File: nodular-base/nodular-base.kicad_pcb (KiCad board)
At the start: 4 copper layers, 83.1 x 92.5 mm, 64 parts, among them J1 Conn_02x10_Counter_Clockwise, J2 Conn_02x10_Counter_Clockwise, J3 Conn_02x10_Counter_Clockwise, J4 Conn_02x10_Counter_Clockwise, J5 Conn_02x10_Counter_Clockwise, J6 Conn_02x10_Counter_Clockwise, J7 USB_C_Receptacle_USB2.0, J8 USB_C_Receptacle_USB2.0, J9 Conn_01x30_MountingPin, SW1 SW_Push, SW2 SW_Push, SW3 SW_Push, U1 ESP32-S3-PICO-1-N8R2, U10 MT9700, U11 MT9700, U12 MT9700, U13 MT9700, U14 MT9700, U2 FUSB302BMPX, U3 BQ25895RTW, U4 TCA9548APWR, U5 MAX3051, U6 74LVC1G17, U7 SC7A20, U8 MT9700, U9 MT9700

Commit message: WIP layout for base
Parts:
- removed the REF** at (99.9, 126.2)
- removed the REF** at (83.7, 100.0)
- removed the REF** at (90.7, 110.5)
- removed the REF** at (113.7, 107.1)
- removed the REF** at (78.8, 112.0)
- removed the REF** at (87.8, 101.5)
- removed the REF** at (79.0, 82.2)
- added C10: 10uF, Capacitor_SMD:C_1206_3216Metric, F.Cu at (119.8, 83.8)
- added C11: 10uF, Capacitor_SMD:C_1206_3216Metric, F.Cu at (122.5, 87.4)
- added C12: 10uF, Capacitor_SMD:C_1206_3216Metric, F.Cu at (118.1, 106.0)
- added C13: 10uF, Capacitor_SMD:C_1206_3216Metric, F.Cu at (119.1, 97.9)
- added C14: 10uF, Capacitor_SMD:C_1206_3216Metric, F.Cu at (118.1, 108.4)
- added C15: 10uF, Capacitor_SMD:C_1206_3216Metric, F.Cu at (120.2, 117.2)
- added C16: 100nF, Capacitor_SMD:C_0402_1005Metric, F.Cu at (126.6, 92.7)
- added C17: 10uF, Capacitor_SMD:C_1206_3216Metric, F.Cu at (102.6, 124.0)
- added C18: 10uF, Capacitor_SMD:C_1206_3216Metric, F.Cu at (96.0, 124.0)
- added C19: 10uF, Capacitor_SMD:C_1206_3216Metric, F.Cu at (80.7, 114.1)
- added C20: 10uF, Capacitor_SMD:C_1206_3216Metric, F.Cu at (77.5, 107.5)
- added C21: 10uF, Capacitor_SMD:C_1206_3216Metric, F.Cu at (83.0, 89.8)
- added C22: 10uF, Capacitor_SMD:C_1206_3216Metric, F.Cu at (82.5, 84.7)
- added C23: 10uF, Capacitor_SMD:C_1206_3216Metric, F.Cu at (86.9, 93.0)
- added C24: 10uF, Capacitor_SMD:C_1206_3216Metric, F.Cu at (87.0, 86.5)
- added C25: 4.7uF, Capacitor_SMD:C_0603_1608Metric, F.Cu at (89.9, 99.2)
- added C26: 47nF, Capacitor_SMD:C_0402_1005Metric, F.Cu at (88.9, 101.0)
- added C27: 10uF, Capacitor_SMD:C_1206_3216Metric, F.Cu at (86.8, 107.8)
- added C28: 10uF, Capacitor_SMD:C_1206_3216Metric, F.Cu at (82.1, 106.8)
- added C29: 10uF, Capacitor_SMD:C_1206_3216Metric, F.Cu at (81.8, 103.3)
- added C30: 1uF, Capacitor_SMD:C_0603_1608Metric, F.Cu at (87.2, 95.8)
- added C31: 47nF, Capacitor_SMD:C_0402_1005Metric, F.Cu at (84.8, 110.2)
- added C32: 10uF, Capacitor_SMD:C_1206_3216Metric, F.Cu at (91.6, 107.8)
- added C33: 10uF, Capacitor_SMD:C_1206_3216Metric, F.Cu at (91.7, 115.3)
- added C34: 10uF, Capacitor_SMD:C_1206_3216Metric, F.Cu at (90.2, 112.9)
- added C9: 22uF, Capacitor_SMD:C_1206_3216Metric, F.Cu at (107.6, 66.9)
- added D2: SK6805MICRO-J, LED_SMD:LED_SK6805_PLCC4_2.4x2.7mm_P1.3mm, F.Cu at (97.0, 80.8)
- added L2: L, Inductor_SMD_Wurth:L_Wurth_WE-LQSH-4020, F.Cu at (86.9, 104.2)
- added L3: L, Inductor_SMD_Wurth:L_Wurth_WE-LQSH-2512, F.Cu at (91.0, 110.3)
- added R10: 10k, Resistor_SMD:R_0402_1005Metric, F.Cu at (126.2, 117.2)
- added R11: 11k3, Resistor_SMD:R_0402_1005Metric, F.Cu at (121.0, 113.6)
- added R12: R, Resistor_SMD:R_0402_1005Metric, F.Cu at (124.5, 83.7)
- added R13: R, Resistor_SMD:R_0603_1608Metric, F.Cu at (127.5, 83.5)
- added R14: 100k, Resistor_SMD:R_0402_1005Metric, F.Cu at (93.3, 130.2)
- added R15: 10k, Resistor_SMD:R_0402_1005Metric, F.Cu at (91.3, 130.2)
- added R16: 11k3, Resistor_SMD:R_0402_1005Metric, F.Cu at (98.2, 125.7)
- added R17: 100k, Resistor_SMD:R_0402_1005Metric, F.Cu at (77.3, 113.7)
- added R18: 10k, Resistor_SMD:R_0402_1005Metric, F.Cu at (72.8, 106.8)
- added R19: 11k3, Resistor_SMD:R_0402_1005Metric, F.Cu at (75.7, 109.7)
- added R20: 100k, Resistor_SMD:R_0402_1005Metric, F.Cu at (75.1, 92.5)
- added R21: 10k, Resistor_SMD:R_0402_1005Metric, F.Cu at (70.1, 92.7)
- added R22: 11k3, Resistor_SMD:R_0402_1005Metric, F.Cu at (80.8, 90.2)
- added R23: 11k3, Resistor_SMD:R_0402_1005Metric, F.Cu at (85.3, 88.6)
- added R24: 1k, Resistor_SMD:R_0402_1005Metric, F.Cu at (97.8, 78.5)
- added R25: 11k3, Resistor_SMD:R_0402_1005Metric, F.Cu at (85.3, 90.7)
- added R26: 1k, Resistor_SMD:R_0402_1005Metric, F.Cu at (99.5, 82.8)
- added R27: 2k2, Resistor_SMD:R_0402_1005Metric, F.Cu at (75.4, 73.7)
- added R28: R, Resistor_SMD:R_0402_1005Metric, F.Cu at (85.8, 110.2)
- added R29: 10k, Resistor_SMD:R_0402_1005Metric, F.Cu at (82.5, 95.5)
- added R3: 11k3, Resistor_SMD:R_0402_1005Metric, F.Cu at (116.2, 87.8)
- added R30: 10k, Resistor_SMD:R_0402_1005Metric, F.Cu at (90.5, 101.0)
- added R31: 10k, Resistor_SMD:R_0402_1005Metric, F.Cu at (91.6, 101.0)
- added R32: R, Resistor_SMD:R_0402_1005Metric, F.Cu at (87.2, 112.1)
- added R4: 100k, Resistor_SMD:R_0402_1005Metric, F.Cu at (116.7, 89.6)
- added R5: 10k, Resistor_SMD:R_0402_1005Metric, F.Cu at (116.7, 90.7)
- added R6: 100k, Resistor_SMD:R_0402_1005Metric, F.Cu at (135.2, 93.9)
- added R7: 10k, Resistor_SMD:R_0402_1005Metric, F.Cu at (132.8, 95.4)
- added R8: 11k3, Resistor_SMD:R_0402_1005Metric, F.Cu at (116.8, 99.5)
- added R9: 100k, Resistor_SMD:R_0402_1005Metric, F.Cu at (124.2, 114.5)
- added REF**: Diodes_UDFN-10_1.0x2.5mm_P0.5mm, Package_DFN_QFN:Diodes_UDFN-10_1.0x2.5mm_P0.5mm, F.Cu at (100.8, 84.2)
- added REF**: Diodes_UDFN-10_1.0x2.5mm_P0.5mm, Package_DFN_QFN:Diodes_UDFN-10_1.0x2.5mm_P0.5mm, F.Cu at (103.9, 84.2)
- added REF**: Diodes_UDFN-10_1.0x2.5mm_P0.5mm, Package_DFN_QFN:Diodes_UDFN-10_1.0x2.5mm_P0.5mm, F.Cu at (93.7, 84.0)
- added REF**: Diodes_UDFN-10_1.0x2.5mm_P0.5mm, Package_DFN_QFN:Diodes_UDFN-10_1.0x2.5mm_P0.5mm, F.Cu at (96.8, 84.0)
- added U15: 74LVC1G04, Package_TO_SOT_SMD:SOT-353_SC-70-5, F.Cu at (119.4, 90.5)
- added U16: RCLAMP0524P-ES, Package_DFN_QFN:Diodes_UDFN-10_1.0x2.5mm_P0.5mm, F.Cu at (106.1, 74.7)
- added U17: RCLAMP0524P-ES, Package_DFN_QFN:Diodes_UDFN-10_1.0x2.5mm_P0.5mm, F.Cu at (120.5, 79.5)
- added U18: RCLAMP0524P-ES, Package_DFN_QFN:Diodes_UDFN-10_1.0x2.5mm_P0.5mm, F.Cu at (109.2, 69.3)
- added U19: 74LVC1G04, Package_TO_SOT_SMD:SOT-353_SC-70-5, F.Cu at (133.2, 93.2)
- added U20: RCLAMP0524P-ES, Package_DFN_QFN:Diodes_UDFN-10_1.0x2.5mm_P0.5mm, F.Cu at (119.3, 93.7)
- added U21: RCLAMP0524P-ES, Package_DFN_QFN:Diodes_UDFN-10_1.0x2.5mm_P0.5mm, F.Cu at (133.0, 101.3)
- added U22: RCLAMP0524P-ES, Package_DFN_QFN:Diodes_UDFN-10_1.0x2.5mm_P0.5mm, F.Cu at (133.0, 98.2)
- added U23: 74LVC1G04, Package_TO_SOT_SMD:SOT-353_SC-70-5, F.Cu at (124.2, 116.8)
- added U24: AW9523B, Package_DFN_QFN:QFN-24-1EP_4x4mm_P0.5mm_EP2.7x2.6mm, F.Cu at (77.2, 120.2)
- added U25: AW9523B, Package_DFN_QFN:QFN-24-1EP_4x4mm_P0.5mm_EP2.7x2.6mm, F.Cu at (125.8, 109.6)
- added U26: AW9523B, Package_DFN_QFN:QFN-24-1EP_4x4mm_P0.5mm_EP2.7x2.6mm, F.Cu at (137.6, 99.9)
- added U27: RCLAMP0524P-ES, Package_DFN_QFN:Diodes_UDFN-10_1.0x2.5mm_P0.5mm, F.Cu at (117.2, 128.8)
- added U28: RCLAMP0524P-ES, Package_DFN_QFN:Diodes_UDFN-10_1.0x2.5mm_P0.5mm, F.Cu at (120.9, 120.4)
- added U29: RCLAMP0524P-ES, Package_DFN_QFN:Diodes_UDFN-10_1.0x2.5mm_P0.5mm, F.Cu at (113.8, 113.1)
- added U30: RCLAMP0524P-ES, Package_DFN_QFN:Diodes_UDFN-10_1.0x2.5mm_P0.5mm, F.Cu at (89.9, 67.2)
- added U31: 74LVC1G04, Package_TO_SOT_SMD:SOT-353_SC-70-5, F.Cu at (95.3, 128.1)
- added U32: 74LVC1G04, Package_TO_SOT_SMD:SOT-353_SC-70-5, F.Cu at (73.5, 108.8)
- added U33: 74LVC1G04, Package_TO_SOT_SMD:SOT-353_SC-70-5, F.Cu at (72.8, 92.0)
- added U34: RCLAMP0524P-ES, Package_DFN_QFN:Diodes_UDFN-10_1.0x2.5mm_P0.5mm, F.Cu at (82.7, 128.5)
- added U35: RCLAMP0524P-ES, Package_DFN_QFN:Diodes_UDFN-10_1.0x2.5mm_P0.5mm, F.Cu at (85.7, 130.4)
- added U36: RCLAMP0524P-ES, Package_DFN_QFN:Diodes_UDFN-10_1.0x2.5mm_P0.5mm, F.Cu at (85.0, 113.2)
- added U37: RCLAMP0524P-ES, Package_DFN_QFN:Diodes_UDFN-10_1.0x2.5mm_P0.5mm, F.Cu at (67.1, 98.5)
- added U38: RCLAMP0524P-ES, Package_DFN_QFN:Diodes_UDFN-10_1.0x2.5mm_P0.5mm, F.Cu at (67.1, 101.8)
- added U39: RCLAMP0524P-ES, Package_DFN_QFN:Diodes_UDFN-10_1.0x2.5mm_P0.5mm, F.Cu at (80.7, 99.3)
- added U40: RCLAMP0524P-ES, Package_DFN_QFN:Diodes_UDFN-10_1.0x2.5mm_P0.5mm, F.Cu at (91.3, 70.0)
- added U41: RCLAMP0524P-ES, Package_DFN_QFN:Diodes_UDFN-10_1.0x2.5mm_P0.5mm, F.Cu at (79.9, 80.0)
- added U42: RCLAMP0524P-ES, Package_DFN_QFN:Diodes_UDFN-10_1.0x2.5mm_P0.5mm, F.Cu at (95.3, 77.3)
- added U43: TLV62595DMQR, nodular:Texas_VSON-HR-6_1.5x1.5mm_P0.5mm, F.Cu at (88.1, 110.0)
- J10: renamed from REF**; value JST_PH_B2B-PH-SM4-TB_1x02-1MP_P2.00mm_Vertical -> Conn_01x02
- moved U4 27.5 mm to (104.5, 131.3), turned to 180 degrees
- moved J3 26.1 mm to (113.0, 122.6), turned to 120 degrees
- moved J6 26.1 mm to (87.0, 77.4), turned to -60 degrees
- moved J1 26.1 mm to (113.0, 77.4), turned to -120 degrees
- moved J2 26.1 mm to (126.1, 100.0), turned to 180 degrees
- moved J4 26.1 mm to (87.0, 122.6), turned to 60 degrees
- moved J5 26.1 mm to (73.9, 100.0), turned to 0 degrees
- moved U11 23.6 mm to (99.3, 123.3)
- moved R2 19.5 mm to (92.0, 65.0), turned to 0 degrees
- moved U3 19.0 mm to (85.7, 99.2), turned to -90 degrees
- moved U13 18.8 mm to (79.8, 87.5), turned to -90 degrees
- moved R1 18.1 mm to (92.0, 66.0), turned to 0 degrees
- moved U6 17.2 mm to (100.6, 79.5), turned to -45 degrees
- moved U9 17.1 mm to (118.5, 102.6), turned to -90 degrees
- moved U10 9.19 mm to (118.8, 112.5), turned to 90 degrees
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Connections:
- net Net-(J7-CC1) renamed /USB/CC1
- net Net-(J7-CC2) renamed /USB/CC2
- net Net-(U3-SYS-Pad15) renamed /USB/VSYS
- C3 pad 1: Net-(U1-VDD3P3_CPU) -> 3V3_SYS
- C4 pad 1: Net-(U1-VDD3P3_CPU) -> 3V3_SYS
- C5 pad 1: Net-(U1-VDD3P3_CPU) -> 3V3_SYS
- C6 pad 1: Net-(U1-VDD3P3_CPU) -> 3V3_SYS
- C7 pad 1: Net-(U1-VDD3P3_CPU) -> 3V3_SYS
- C8 pad 1: Net-(U1-VDD3P3_CPU) -> 3V3_SYS
- D1 pad 1: unconnected-(D1-K-Pad1) -> /USB/STAT
- D1 pad 2: unconnected-(D1-A-Pad2) -> Net-(D1-A)
- J1 pad 12: unconnected-(J1-Pin_12-Pad12) -> /NA_HS1
- J1 pad 13: unconnected-(J1-Pin_13-Pad13) -> /NA_HS2
- J1 pad 15: unconnected-(J1-Pin_15-Pad15) -> /SFPs/PORTA_3V3
- J1 pad 16: unconnected-(J1-Pin_16-Pad16) -> /SFPs/PORTA_3V3
- J1 pad 18: unconnected-(J1-Pin_18-Pad18) -> /NA_HS3
- J1 pad 19: unconnected-(J1-Pin_19-Pad19) -> /NA_HS4
- J1 pad 2: unconnected-(J1-Pin_2-Pad2) -> /GPIO/ALS1
- J1 pad 3: unconnected-(J1-Pin_3-Pad3) -> /GPIO/ALS2
- J1 pad 4: unconnected-(J1-Pin_4-Pad4) -> /I2C/SDA_A
- J1 pad 5: unconnected-(J1-Pin_5-Pad5) -> /I2C/SCL_A
- J1 pad 6: unconnected-(J1-Pin_6-Pad6) -> /SFPs/A_NDET
- J1 pad 7: unconnected-(J1-Pin_7-Pad7) -> /GPIO/ALS3
- J1 pad 8: unconnected-(J1-Pin_8-Pad8) -> /GPIO/ALS4
- J1 pad 9: unconnected-(J1-Pin_9-Pad9) -> /GPIO/ALS5
- J10 pad 1: (no net) -> /USB/BAT+
- J10 pad 2: (no net) -> GND
- J2 pad 12: unconnected-(J2-Pin_12-Pad12) -> /NB_HS1
- J2 pad 13: unconnected-(J2-Pin_13-Pad13) -> /NB_HS2
- J2 pad 15: unconnected-(J2-Pin_15-Pad15) -> /SFPs/PORTB_3V3
- J2 pad 16: unconnected-(J2-Pin_16-Pad16) -> /SFPs/PORTB_3V3
- J2 pad 18: unconnected-(J2-Pin_18-Pad18) -> /NB_HS3
- J2 pad 19: unconnected-(J2-Pin_19-Pad19) -> /NB_HS4
- J2 pad 2: unconnected-(J2-Pin_2-Pad2) -> /GPIO/BLS1
- J2 pad 3: unconnected-(J2-Pin_3-Pad3) -> /GPIO/BLS2
- J2 pad 4: unconnected-(J2-Pin_4-Pad4) -> /I2C/SDA_B
- J2 pad 5: unconnected-(J2-Pin_5-Pad5) -> /I2C/SCL_B
- J2 pad 6: unconnected-(J2-Pin_6-Pad6) -> /SFPs/B_NDET
- J2 pad 7: unconnected-(J2-Pin_7-Pad7) -> /GPIO/BLS3
- J2 pad 8: unconnected-(J2-Pin_8-Pad8) -> /GPIO/BLS4
- J2 pad 9: unconnected-(J2-Pin_9-Pad9) -> /GPIO/BLS5
- J3 pad 12: unconnected-(J3-Pin_12-Pad12) -> /NC_HS1
- J3 pad 13: unconnected-(J3-Pin_13-Pad13) -> /NC_HS2
- J3 pad 15: unconnected-(J3-Pin_15-Pad15) -> /SFPs/PORTC_3V3
- J3 pad 16: unconnected-(J3-Pin_16-Pad16) -> /SFPs/PORTC_3V3
- J3 pad 18: unconnected-(J3-Pin_18-Pad18) -> /NC_HS3
- J3 pad 19: unconnected-(J3-Pin_19-Pad19) -> /NC_HS4
- J3 pad 2: unconnected-(J3-Pin_2-Pad2) -> /GPIO/CLS1
- J3 pad 3: unconnected-(J3-Pin_3-Pad3) -> /GPIO/CLS2
- J3 pad 4: unconnected-(J3-Pin_4-Pad4) -> /I2C/SDA_C
- J3 pad 5: unconnected-(J3-Pin_5-Pad5) -> /I2C/SCL_C
- J3 pad 6: unconnected-(J3-Pin_6-Pad6) -> /SFPs/C_NDET
- J3 pad 7: unconnected-(J3-Pin_7-Pad7) -> /GPIO/CLS3
- J3 pad 8: unconnected-(J3-Pin_8-Pad8) -> /GPIO/CLS4
- J3 pad 9: unconnected-(J3-Pin_9-Pad9) -> /GPIO/CLS5
- J4 pad 12: unconnected-(J4-Pin_12-Pad12) -> /ND_HS1
- J4 pad 13: unconnected-(J4-Pin_13-Pad13) -> /ND_HS2
- J4 pad 15: unconnected-(J4-Pin_15-Pad15) -> /SFPs/PORTD_3V3
- J4 pad 16: unconnected-(J4-Pin_16-Pad16) -> /SFPs/PORTD_3V3
- J4 pad 18: unconnected-(J4-Pin_18-Pad18) -> /ND_HS3
- J4 pad 19: unconnected-(J4-Pin_19-Pad19) -> /ND_HS4
- J4 pad 2: unconnected-(J4-Pin_2-Pad2) -> /GPIO/DLS1
- J4 pad 3: unconnected-(J4-Pin_3-Pad3) -> /GPIO/DLS2
- J4 pad 4: unconnected-(J4-Pin_4-Pad4) -> /I2C/SDA_D
- J4 pad 5: unconnected-(J4-Pin_5-Pad5) -> /I2C/SCL_D
- J4 pad 6: unconnected-(J4-Pin_6-Pad6) -> /SFPs/D_NDET
- J4 pad 7: unconnected-(J4-Pin_7-Pad7) -> /GPIO/DLS3
- J4 pad 8: unconnected-(J4-Pin_8-Pad8) -> /GPIO/DLS4
- J4 pad 9: unconnected-(J4-Pin_9-Pad9) -> /GPIO/DLS5
- J5 pad 12: unconnected-(J5-Pin_12-Pad12) -> /NE_HS1
- J5 pad 13: unconnected-(J5-Pin_13-Pad13) -> /NE_HS2
- J5 pad 15: unconnected-(J5-Pin_15-Pad15) -> /SFPs/PORTE_3V3
- J5 pad 16: unconnected-(J5-Pin_16-Pad16) -> /SFPs/PORTE_3V3
- J5 pad 18: unconnected-(J5-Pin_18-Pad18) -> /NE_HS3
- J5 pad 19: unconnected-(J5-Pin_19-Pad19) -> /NE_HS4
- J5 pad 2: unconnected-(J5-Pin_2-Pad2) -> /GPIO/ELS1
- J5 pad 3: unconnected-(J5-Pin_3-Pad3) -> /GPIO/ELS2
- J5 pad 4: unconnected-(J5-Pin_4-Pad4) -> /I2C/SDA_E
- J5 pad 5: unconnected-(J5-Pin_5-Pad5) -> /I2C/SCL_E
- J5 pad 6: unconnected-(J5-Pin_6-Pad6) -> /SFPs/E_NDET
- J5 pad 7: unconnected-(J5-Pin_7-Pad7) -> /GPIO/ELS3
- J5 pad 8: unconnected-(J5-Pin_8-Pad8) -> /GPIO/ELS4
- J5 pad 9: unconnected-(J5-Pin_9-Pad9) -> /GPIO/ELS5
- J6 pad 12: unconnected-(J6-Pin_12-Pad12) -> /NF_HS1
- J6 pad 13: unconnected-(J6-Pin_13-Pad13) -> /NF_HS2
- J6 pad 15: unconnected-(J6-Pin_15-Pad15) -> /SFPs/PORTF_3V3
- J6 pad 16: unconnected-(J6-Pin_16-Pad16) -> /SFPs/PORTF_3V3
- J6 pad 18: unconnected-(J6-Pin_18-Pad18) -> /NF_HS3
- J6 pad 19: unconnected-(J6-Pin_19-Pad19) -> /NF_HS4
- J6 pad 2: unconnected-(J6-Pin_2-Pad2) -> /GPIO/FLS1
- J6 pad 3: unconnected-(J6-Pin_3-Pad3) -> /GPIO/FLS2
- J6 pad 4: unconnected-(J6-Pin_4-Pad4) -> /I2C/SDA_F
- J6 pad 5: unconnected-(J6-Pin_5-Pad5) -> /I2C/SCL_F
- J6 pad 6: unconnected-(J6-Pin_6-Pad6) -> /SFPs/F_NDET
- J6 pad 7: unconnected-(J6-Pin_7-Pad7) -> /GPIO/FLS3
- J6 pad 8: unconnected-(J6-Pin_8-Pad8) -> /GPIO/FLS4
- J6 pad 9: unconnected-(J6-Pin_9-Pad9) -> /GPIO/FLS5
- J7 pad A4: Net-(U2-VBUS) -> /USB/VBUS
- J7 pad A9: Net-(U2-VBUS) -> /USB/VBUS
- J7 pad B4: Net-(U2-VBUS) -> /USB/VBUS
- J7 pad B9: Net-(U2-VBUS) -> /USB/VBUS
- J8 pad A1: Net-(J8-GND-PadA1) -> GND
- J8 pad A12: Net-(J8-GND-PadA1) -> GND
- J8 pad A4: Net-(J8-VBUS-PadA4) -> unconnected-(J8-VBUS-PadA4)
- J8 pad A6: unconnected-(J8-D+-PadA6) -> Net-(J8-D+-PadA6)
- J8 pad A7: unconnected-(J8-D--PadA7) -> Net-(J8-D--PadA7)
- J8 pad A9: Net-(J8-VBUS-PadA4) -> unconnected-(J8-VBUS-PadA4)
- J8 pad B1: Net-(J8-GND-PadA1) -> GND
- J8 pad B12: Net-(J8-GND-PadA1) -> GND
- J8 pad B4: Net-(J8-VBUS-PadA4) -> unconnected-(J8-VBUS-PadA4)
- J8 pad B6: unconnected-(J8-D+-PadB6) -> Net-(J8-D+-PadA6)
- J8 pad B7: unconnected-(J8-D--PadB7) -> Net-(J8-D--PadA7)
- J8 pad B9: Net-(J8-VBUS-PadA4) -> unconnected-(J8-VBUS-PadA4)
- J8 pad S1: unconnected-(J8-SHIELD-PadS1) -> GND
- U1 pad 10: unconnected-(U1-GPIO5-Pad10) -> /NF_HS3
- U1 pad 11: unconnected-(U1-GPIO6-Pad11) -> /NF_HS4
- U1 pad 16: unconnected-(U1-GPIO11-Pad16) -> /ND_HS1
- U1 pad 17: unconnected-(U1-GPIO12-Pad17) -> /ND_HS4
- U1 pad 18: unconnected-(U1-GPIO13-Pad18) -> /ND_HS3
- U1 pad 19: unconnected-(U1-GPIO14-Pad19) -> /ND_HS2
- U1 pad 2: Net-(U1-VDD3P3_CPU) -> 3V3_SYS
- U1 pad 20: Net-(U1-VDD3P3_CPU) -> 3V3_SYS
- U1 pad 21: unconnected-(U1-GPIO15-Pad21) -> /NE_HS3
- U1 pad 22: unconnected-(U1-GPIO16-Pad22) -> /NE_HS2
- U1 pad 23: unconnected-(U1-GPIO17-Pad23) -> /NE_HS4
- U1 pad 24: unconnected-(U1-GPIO18-Pad24) -> /NE_HS1
- U1 pad 27: unconnected-(U1-GPIO21-Pad27) -> /LED_DATA
- U1 pad 3: Net-(U1-VDD3P3_CPU) -> 3V3_SYS
- U1 pad 36: unconnected-(U1-GPIO48/SPICLK_n-Pad36) -> /NC_HS4
- U1 pad 37: unconnected-(U1-GPIO47/SPICLK_P-Pad37) -> /NC_HS3
- U1 pad 38: unconnected-(U1-GPIO33-Pad38) -> /NC_HS2
- U1 pad 39: unconnected-(U1-GPIO34-Pad39) -> /NC_HS1
- U1 pad 40: unconnected-(U1-GPIO35-Pad40) -> /NB_HS1
- U1 pad 41: unconnected-(U1-GPIO36-Pad41) -> /NB_HS2
- U1 pad 42: unconnected-(U1-GPIO37-Pad42) -> /NB_HS3
- U1 pad 43: unconnected-(U1-GPIO38-Pad43) -> /NB_HS4
- U1 pad 44: unconnected-(U1-GPIO39/MTCK-Pad44) -> /NA_HS1
- U1 pad 45: unconnected-(U1-GPIO40/MTDO-Pad45) -> /NA_HS2
- U1 pad 46: Net-(U1-VDD3P3_CPU) -> 3V3_SYS
- U1 pad 47: unconnected-(U1-GPIO41/MTDI-Pad47) -> /NA_HS3
- U1 pad 48: unconnected-(U1-GPIO42/MTMS-Pad48) -> /NA_HS4
- U1 pad 55: Net-(U1-VDD3P3_CPU) -> 3V3_SYS
- U1 pad 56: Net-(U1-VDD3P3_CPU) -> 3V3_SYS
- U1 pad 8: unconnected-(U1-GPIO3-Pad8) -> /NF_HS1
- U1 pad 9: unconnected-(U1-GPIO4-Pad9) -> /NF_HS2
- U10 pad 1: unconnected-(U10-OUT-Pad1) -> /SFPs/PORTC_3V3
- U10 pad 2: unconnected-(U10-GND-Pad2) -> GND
- U10 pad 3: unconnected-(U10-SET-Pad3) -> Net-(U10-SET)
- U10 pad 4: unconnected-(U10-ON-Pad4) -> /SFPs/C_LSEN
- U10 pad 5: unconnected-(U10-IN-Pad5) -> 3V3_SYS
- U11 pad 1: unconnected-(U11-OUT-Pad1) -> /SFPs/PORTD_3V3
- U11 pad 2: unconnected-(U11-GND-Pad2) -> GND
- U11 pad 3: unconnected-(U11-SET-Pad3) -> Net-(U11-SET)
- U11 pad 4: unconnected-(U11-ON-Pad4) -> /SFPs/D_LSEN
- U11 pad 5: unconnected-(U11-IN-Pad5) -> 3V3_SYS
- U12 pad 1: unconnected-(U12-OUT-Pad1) -> /SFPs/PORTE_3V3
- U12 pad 2: unconnected-(U12-GND-Pad2) -> GND
- U12 pad 3: unconnected-(U12-SET-Pad3) -> Net-(U12-SET)
- U12 pad 4: unconnected-(U12-ON-Pad4) -> /SFPs/E_LSEN
- U12 pad 5: unconnected-(U12-IN-Pad5) -> 3V3_SYS
- U13 pad 1: unconnected-(U13-OUT-Pad1) -> /SFPs/PORTF_3V3
- U13 pad 2: unconnected-(U13-GND-Pad2) -> GND
- U13 pad 3: unconnected-(U13-SET-Pad3) -> Net-(U13-SET)
- U13 pad 4: unconnected-(U13-ON-Pad4) -> /SFPs/F_LSEN
- U13 pad 5: unconnected-(U13-IN-Pad5) -> 3V3_SYS
- U14 pad 1: unconnected-(U14-OUT-Pad1) -> /bot-top-link/TOP_VBAT_SW
- U14 pad 2: unconnected-(U14-GND-Pad2) -> GND
- U14 pad 3: unconnected-(U14-SET-Pad3) -> Net-(U14-SET)
- U14 pad 4: unconnected-(U14-ON-Pad4) -> /GPIO/LED_PWR_EN
- U14 pad 5: unconnected-(U14-IN-Pad5) -> Net-(U14-IN)
- U2 pad 15: Net-(U2-GND-Pad15) -> GND
- U2 pad 2: Net-(U2-VBUS) -> /USB/VBUS
- U2 pad 3: Net-(U2-VDD-Pad3) -> 3V3_SYS
- U2 pad 4: Net-(U2-VDD-Pad3) -> 3V3_SYS
- U2 pad 6: unconnected-(U2-SCL-Pad6) -> /SCL_SYS
- U2 pad 7: unconnected-(U2-SDA-Pad7) -> /SDA_SYS
- U2 pad 8: Net-(U2-GND-Pad15) -> GND
- U2 pad 9: Net-(U2-GND-Pad15) -> GND
- U3 pad 1: unconnected-(U3-VBUS-Pad1) -> /USB/VBUS
- U3 pad 10: unconnected-(U3-ILIM-Pad10) -> Net-(U3-ILIM)
- U3 pad 11: unconnected-(U3-TS-Pad11) -> Net-(U3-TS)
- U3 pad 12: unconnected-(U3-~{QON}-Pad12) -> /USB/~{QON}
- U3 pad 13: Net-(U3-BAT-Pad13) -> /USB/BAT+
- U3 pad 14: Net-(U3-BAT-Pad13) -> /USB/BAT+
- U3 pad 17: Net-(U3-PGND-Pad17) -> GND
- U3 pad 18: Net-(U3-PGND-Pad17) -> GND
- U3 pad 21: unconnected-(U3-BTST-Pad21) -> Net-(U3-BTST)
- U3 pad 22: unconnected-(U3-REGN-Pad22) -> Net-(U3-REGN)
- U3 pad 25: Net-(U3-PGND-Pad17) -> GND
- U3 pad 4: unconnected-(U3-STAT-Pad4) -> /USB/STAT
- U3 pad 5: unconnected-(U3-SCL-Pad5) -> /SCL_SYS
- U3 pad 6: unconnected-(U3-SDA-Pad6) -> /SDA_SYS
- U3 pad 9: unconnected-(U3-~{CE}-Pad9) -> GND
- U4 pad 10: unconnected-(U4-SD3-Pad10) -> /I2C/SDA_C
- U4 pad 11: unconnected-(U4-SC3-Pad11) -> /I2C/SCL_C
- U4 pad 12: unconnected-(U4-GND-Pad12) -> GND
- U4 pad 13: unconnected-(U4-SD4-Pad13) -> /I2C/SDA_D
- U4 pad 14: unconnected-(U4-SC4-Pad14) -> /I2C/SCL_D
- U4 pad 15: unconnected-(U4-SD5-Pad15) -> /I2C/SDA_E
- U4 pad 16: unconnected-(U4-SC5-Pad16) -> /I2C/SCL_E
- U4 pad 17: unconnected-(U4-SD6-Pad17) -> /I2C/SDA_F
- U4 pad 18: unconnected-(U4-SC6-Pad18) -> /I2C/SCL_F
- U4 pad 4: unconnected-(U4-SD0-Pad4) -> /SDA_SYS
- U4 pad 5: unconnected-(U4-SC0-Pad5) -> /SCL_SYS
- U4 pad 6: unconnected-(U4-SD1-Pad6) -> /I2C/SDA_A
- U4 pad 7: unconnected-(U4-SC1-Pad7) -> /I2C/SCL_A
- U4 pad 8: unconnected-(U4-SD2-Pad8) -> /I2C/SDA_B
- U4 pad 9: unconnected-(U4-SC2-Pad9) -> /I2C/SCL_B
- U5 pad 2: unconnected-(U5-GND-Pad2) -> GND
- U5 pad 3: unconnected-(U5-VDD-Pad3) -> Net-(U5-VDD)
- U5 pad 7: unconnected-(U5-CANH-Pad7) -> Net-(U5-CANH)
- U5 pad 8: unconnected-(U5-RS-Pad8) -> Net-(U5-RS)
- U6 pad 2: unconnected-(U6-Pad2) -> /LED_DATA
- U6 pad 3: unconnected-(U6-GND-Pad3) -> GND
- U6 pad 4: unconnected-(U6-Pad4) -> Net-(R24-Pad1)
- U6 pad 5: unconnected-(U6-VCC-Pad5) -> /bot-top-link/TOP_VBAT_SW
- U8 pad 1: unconnected-(U8-OUT-Pad1) -> /SFPs/PORTA_3V3
- U8 pad 2: unconnected-(U8-GND-Pad2) -> GND
- U8 pad 3: unconnected-(U8-SET-Pad3) -> Net-(U8-SET)
- U8 pad 4: unconnected-(U8-ON-Pad4) -> /SFPs/A_LSEN
- U8 pad 5: unconnected-(U8-IN-Pad5) -> 3V3_SYS
- U9 pad 1: unconnected-(U9-OUT-Pad1) -> /SFPs/PORTB_3V3
- U9 pad 2: unconnected-(U9-GND-Pad2) -> GND
- U9 pad 3: unconnected-(U9-SET-Pad3) -> Net-(U9-SET)
- U9 pad 4: unconnected-(U9-ON-Pad4) -> /SFPs/B_LSEN
- U9 pad 5: unconnected-(U9-IN-Pad5) -> 3V3_SYS
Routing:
- net 3V3_SYS: track 0.00 -> 369.7 mm, vias 0 -> 25
- net GND: track 2.08 -> 218.6 mm, vias 1 -> 127
- net /SDA_SYS: track 0.00 -> 162.2 mm, vias 0 -> 11
- net /SCL_SYS: track 0.00 -> 162.1 mm, vias 0 -> 11
- net /GPIO/DET_F: track 0.00 -> 133.8 mm, vias 0 -> 6
- net /I2C/SCL_F: track 0.00 -> 115.2 mm, vias 0 -> 2
- net /I2C/SDA_F: track 0.00 -> 114.7 mm, vias 0 -> 2
- net /~{INT_SYS}: track 0.00 -> 104.1 mm, vias 0 -> 5
- net /GPIO/DET_E: track 0.00 -> 103.6 mm, vias 0 -> 6
- net /I2C/SDA_A: track 0.00 -> 85.6 mm, vias 0 -> 4
- net /I2C/SCL_A: track 0.00 -> 84.7 mm, vias 0 -> 4
- net /ND_HS1: track 0.00 -> 76.1 mm, vias 0 -> 2
- net /ND_HS2: track 0.00 -> 73.9 mm, vias 0 -> 2
- net /GPIO/FLS1: track 0.00 -> 73.1 mm, vias 0 -> 2
- net /ND_HS4: track 0.00 -> 72.9 mm, vias 0 -> 2
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- added copper zone on B.Cu, net GND
- added copper zone on F.Cu, net GND
- added copper zone on In1.Cu, net GND
- added copper zone on In2.Cu, net GND

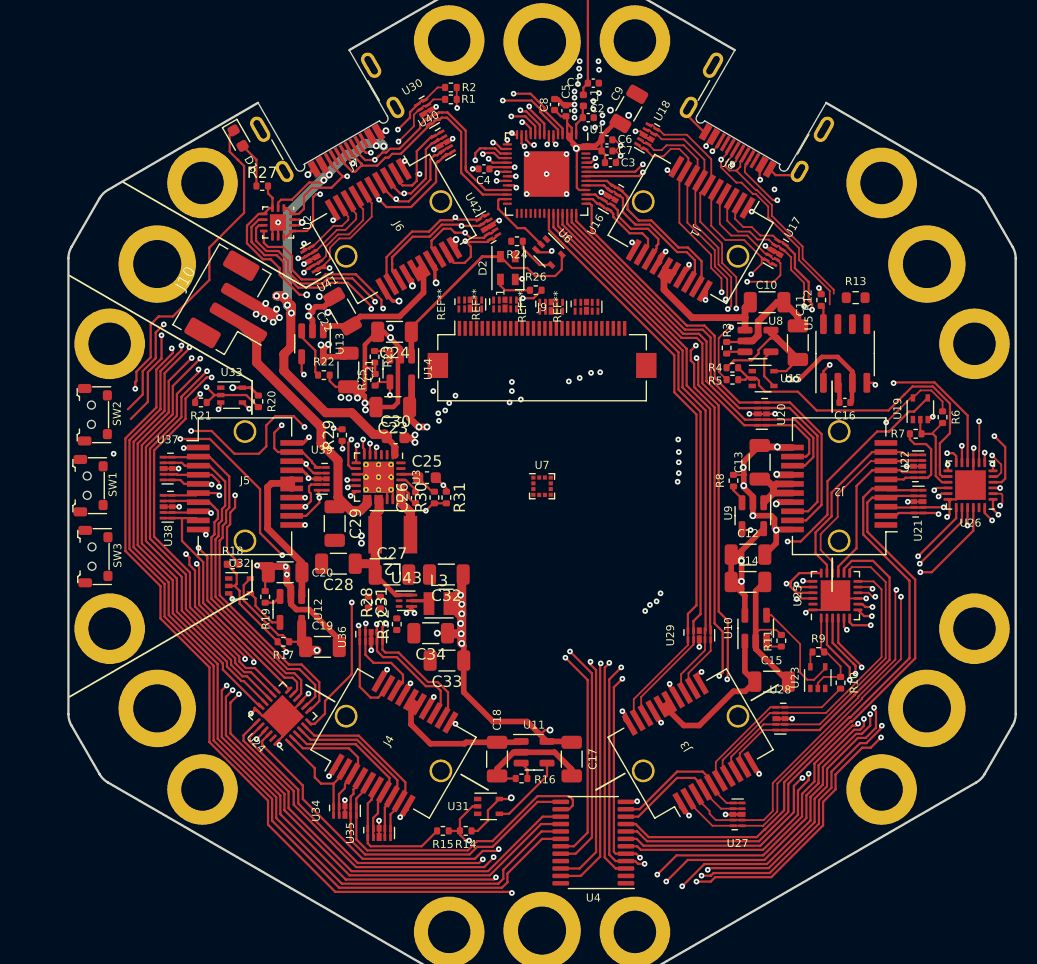
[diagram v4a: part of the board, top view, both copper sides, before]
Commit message: Switched from CAN to USB for second USB-C port Added second PD controller and USB mux to allow switching between host and device port Added SOICbite to corner All routing complete Updated pin map, added i2c addresses, soicbit pin mapping, and fpc pinout to document
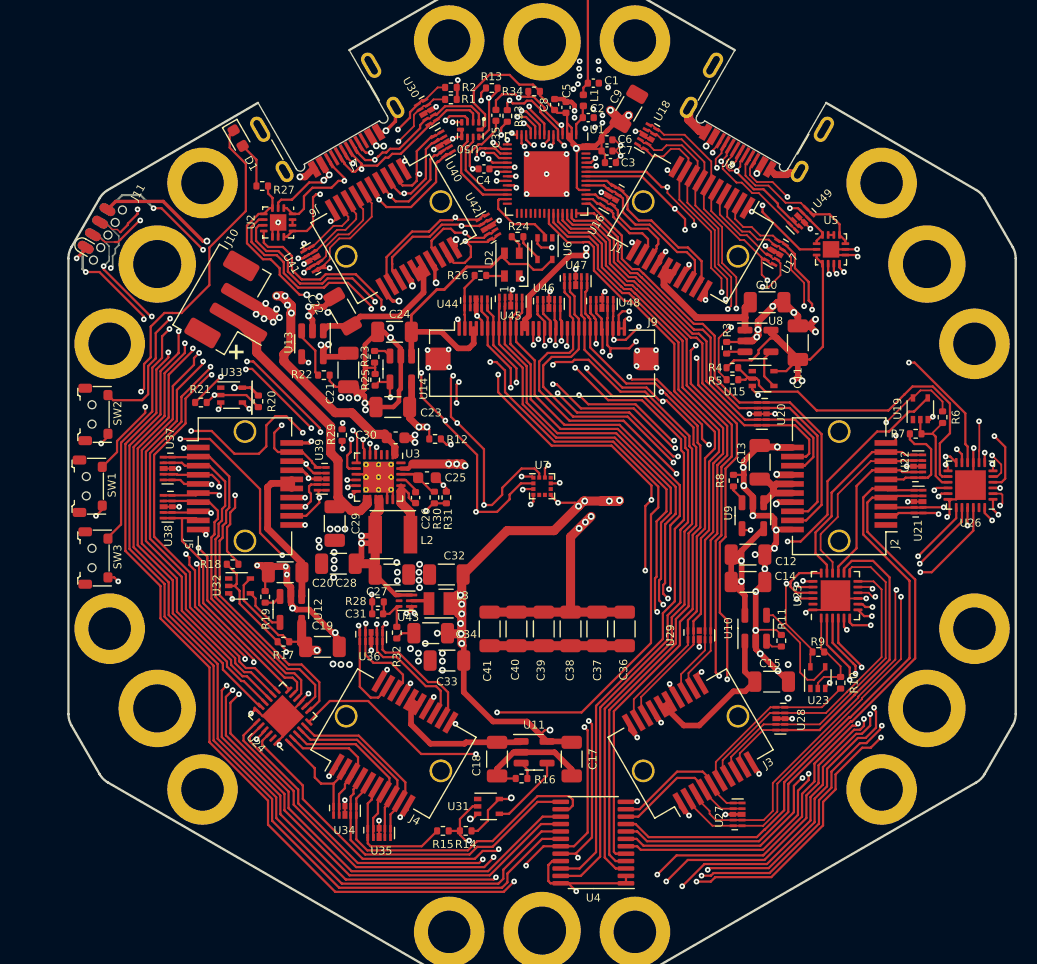
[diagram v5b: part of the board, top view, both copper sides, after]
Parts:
- removed C16: 100nF, Capacitor_SMD:C_0402_1005Metric
- removed REF** (x4): Diodes_UDFN-10_1.0x2.5mm_P0.5mm, Package_DFN_QFN:Diodes_UDFN-10_1.0x2.5mm_P0.5mm
- added C35: 100nF, Capacitor_SMD:C_0402_1005Metric, F.Cu at (96.0, 67.5)
- added C36: 10uF, Capacitor_SMD:C_1206_3216Metric, F.Cu at (107.2, 112.5)
- added C37: 10uF, Capacitor_SMD:C_1206_3216Metric, F.Cu at (104.8, 112.5)
- added C38: 10uF, Capacitor_SMD:C_1206_3216Metric, F.Cu at (102.5, 112.5)
- added C39: 10uF, Capacitor_SMD:C_1206_3216Metric, F.Cu at (100.2, 112.5)
- added C40: 10uF, Capacitor_SMD:C_1206_3216Metric, F.Cu at (97.8, 112.5)
- added C41: 10uF, Capacitor_SMD:C_1206_3216Metric, F.Cu at (95.4, 112.5)
- added J11: Conn_01x08_Pin, nodular:SOIC_clipProgSmall, F.Cu at (60.2, 77.0)
- added R33: 10k, Resistor_SMD:R_0402_1005Metric, F.Cu at (97.0, 67.5)
- added R34: 10k, Resistor_SMD:R_0402_1005Metric, F.Cu at (99.3, 65.3)
- added U44: RCLAMP0524P-ES, Package_DFN_QFN:Diodes_UDFN-10_1.0x2.5mm_P0.5mm, F.Cu at (94.2, 84.0)
- added U45: RCLAMP0524P-ES, Package_DFN_QFN:Diodes_UDFN-10_1.0x2.5mm_P0.5mm, F.Cu at (97.2, 83.8)
- added U46: RCLAMP0524P-ES, Package_DFN_QFN:Diodes_UDFN-10_1.0x2.5mm_P0.5mm, F.Cu at (100.6, 84.0)
- added U47: RCLAMP0524P-ES, Package_DFN_QFN:Diodes_UDFN-10_1.0x2.5mm_P0.5mm, F.Cu at (103.0, 82.0)
- added U48: RCLAMP0524P-ES, Package_DFN_QFN:Diodes_UDFN-10_1.0x2.5mm_P0.5mm, F.Cu at (105.2, 84.0)
- added U49: RCLAMP0524P-ES, Package_DFN_QFN:Diodes_UDFN-10_1.0x2.5mm_P0.5mm, F.Cu at (122.7, 76.6)
- added U50: TS3USB221A, nodular:Texas_PUQFN-10_RSE_1.5x2mm, F.Cu at (93.7, 68.7)
- J10: value Conn_01x02 -> Conn_01x02_MountingPin
- J9: footprint Connector_FFC-FPC:Hirose_FH12-30S-0.5SH_1x30-1MP_P0.50mm_Horizontal -> nodular:Jushuo_AFC01-S30FCC-00_1x30-1MP_P0.50mm_Horizontal
- R12: value R -> 1k
- R13: value R -> 10k; footprint Resistor_SMD:R_0603_1608Metric -> Resistor_SMD:R_0402_1005Metric
- U5: value MAX3051 -> FUSB302BMPX; footprint Package_SO:SO-8_3.9x4.9mm_P1.27mm -> Package_DFN_QFN:WQFN-14-1EP_2.5x2.5mm_P0.5mm_EP1.45x1.45mm
- moved R13 36.9 mm to (95.6, 65.0)
- moved R12 36.0 mm to (90.6, 95.8), turned to 180 degrees
- moved U5 9.22 mm to (125.4, 79.2), turned to 0 degrees
- moved R26 5.03 mm to (94.6, 81.5), turned to 180 degrees
- moved C31 1.32 mm to (85.6, 111.2), turned to 0 degrees
- moved J9 1.23 mm to (100.0, 89.2)
- moved R32 0.74 mm to (87.2, 112.8)
- moved D2 0.46 mm to (97.3, 80.5)
- moved U6 0.46 mm to (100.2, 79.2), turned to -90 degrees
- moved R24 0.40 mm to (97.8, 78.1)
- moved C5 0.30 mm to (102.1, 66.8)
- moved R28 0.21 mm to (85.6, 110.2), turned to 180 degrees
- moved SW3 0.12 mm to (60.5, 106.3)
- moved SW1 0.09 mm to (60.0, 100.0)
- moved SW2 0.06 mm to (60.5, 93.7)
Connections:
- net /USB/VBUS renamed /VBUS
- net Net-(J8-D+-PadA6) renamed /USB/HOST_D+
- net Net-(J8-D--PadA7) renamed /USB/HOST_D-
- C23 pad 1: Net-(U14-IN) -> /VSYS
- C27 pad 1: /USB/VSYS -> /VSYS
- C28 pad 1: /USB/VSYS -> /VSYS
- J10 pad MP: (no net) -> GND
- J7 pad A6: /USB+ -> /DEV_USB+
- J7 pad A7: /USB- -> /DEV_USB-
- J7 pad B6: /USB+ -> /DEV_USB+
- J7 pad B7: /USB- -> /DEV_USB-
- J8 pad A4: unconnected-(J8-VBUS-PadA4) -> /USB/PMID
- J8 pad A5: unconnected-(J8-CC1-PadA5) -> Net-(J8-CC1)
- J8 pad A8: unconnected-(J8-SBU1-PadA8) -> /ESP_TXD
- J8 pad A9: unconnected-(J8-VBUS-PadA4) -> /USB/PMID
- J8 pad B4: unconnected-(J8-VBUS-PadA4) -> /USB/PMID
- J8 pad B5: unconnected-(J8-CC2-PadB5) -> Net-(J8-CC2)
- J8 pad B8: unconnected-(J8-SBU2-PadB8) -> /ESP_RXD
- J8 pad B9: unconnected-(J8-VBUS-PadA4) -> /USB/PMID
- J9 pad 1: unconnected-(J9-Pin_1-Pad1) -> GND
- J9 pad 10: unconnected-(J9-Pin_10-Pad10) -> /GPIO/BTN5
- J9 pad 11: unconnected-(J9-Pin_11-Pad11) -> /GPIO/BTN6
- J9 pad 12: unconnected-(J9-Pin_12-Pad12) -> 3V3_SYS
- J9 pad 13: unconnected-(J9-Pin_13-Pad13) -> 3V3_SYS
- J9 pad 14: unconnected-(J9-Pin_14-Pad14) -> GND
- J9 pad 15: unconnected-(J9-Pin_15-Pad15) -> GND
- J9 pad 16: unconnected-(J9-Pin_16-Pad16) -> /TOP_HS1
- J9 pad 17: unconnected-(J9-Pin_17-Pad17) -> /TOP_HS2
- J9 pad 18: unconnected-(J9-Pin_18-Pad18) -> /TOP_HS3
- J9 pad 19: unconnected-(J9-Pin_19-Pad19) -> /TOP_HS4
- J9 pad 2: unconnected-(J9-Pin_2-Pad2) -> /bot-top-link/LED_DATA_TOP
- J9 pad 20: unconnected-(J9-Pin_20-Pad20) -> GND
- J9 pad 21: unconnected-(J9-Pin_21-Pad21) -> /GPIO/TLS1
- J9 pad 22: unconnected-(J9-Pin_22-Pad22) -> /GPIO/TLS2
- J9 pad 23: unconnected-(J9-Pin_23-Pad23) -> /SDA_TOP
- J9 pad 24: unconnected-(J9-Pin_24-Pad24) -> /SCL_TOP
- J9 pad 25: unconnected-(J9-Pin_25-Pad25) -> /~{BOOTLOADER}
- J9 pad 26: unconnected-(J9-Pin_26-Pad26) -> /~{ESPRESET}
- J9 pad 27: unconnected-(J9-Pin_27-Pad27) -> /ESP_TXD
- J9 pad 28: unconnected-(J9-Pin_28-Pad28) -> /ESP_RXD
- J9 pad 29: unconnected-(J9-Pin_29-Pad29) -> GND
- J9 pad 3: unconnected-(J9-Pin_3-Pad3) -> /bot-top-link/TOP_VBAT_SW
- J9 pad 30: unconnected-(J9-Pin_30-Pad30) -> GND
- J9 pad 4: unconnected-(J9-Pin_4-Pad4) -> /bot-top-link/TOP_VBAT_SW
- J9 pad 5: unconnected-(J9-Pin_5-Pad5) -> GND
- J9 pad 6: unconnected-(J9-Pin_6-Pad6) -> /GPIO/BTN1
- J9 pad 7: unconnected-(J9-Pin_7-Pad7) -> /GPIO/BTN2
- J9 pad 8: unconnected-(J9-Pin_8-Pad8) -> /GPIO/BTN3
- J9 pad 9: unconnected-(J9-Pin_9-Pad9) -> /GPIO/BTN4
- L2 pad 2: /USB/VSYS -> /VSYS
- R12 pad 1: Net-(U5-RS) -> /USB/PMIC_OTG
- R12 pad 2: GND -> /VSYS
- R13 pad 1: Net-(U5-CANH) -> GND
- R13 pad 2: unconnected-(R13-Pad2) -> /USBSEL
- SW1 pad 1: unconnected-(SW1-Pad1) -> GND
- SW1 pad 2: unconnected-(SW1-Pad2) -> /~{QON}
- SW2 pad 1: unconnected-(SW2-Pad1) -> GND
- SW2 pad 2: unconnected-(SW2-Pad2) -> /~{ESPRESET}
- SW3 pad 1: unconnected-(SW3-Pad1) -> GND
- SW3 pad 2: unconnected-(SW3-Pad2) -> /~{BOOTLOADER}
- U1 pad 12: unconnected-(U1-GPIO7-Pad12) -> /TOP_HS2
- U1 pad 13: unconnected-(U1-GPIO8-Pad13) -> /TOP_HS1
- U1 pad 14: unconnected-(U1-GPIO9-Pad14) -> /I2C_RESET
- U1 pad 15: unconnected-(U1-GPIO10-Pad15) -> /~{INT_SYS}
- U1 pad 4: unconnected-(U1-CHIP_PU-Pad4) -> /~{ESPRESET}
- U1 pad 49: unconnected-(U1-U0TXD-Pad49) -> /ESP_TXD
- U1 pad 5: unconnected-(U1-GPIO0-Pad5) -> /~{BOOTLOADER}
- U1 pad 50: unconnected-(U1-U0RXD-Pad50) -> /ESP_RXD
- U1 pad 51: unconnected-(U1-GPIO45-Pad51) -> /SDA_HOST
- U1 pad 52: unconnected-(U1-GPIO46-Pad52) -> /SCL_HOST
- U1 pad 6: unconnected-(U1-GPIO1-Pad6) -> /TOP_HS4
- U1 pad 7: unconnected-(U1-GPIO2-Pad7) -> /TOP_HS3
- U14 pad 5: Net-(U14-IN) -> /VSYS
- U2 pad 5: unconnected-(U2-INT_N-Pad5) -> /~{INT_SYS}
- U26 pad 10: /GPIO/CAN_EN -> unconnected-(U26-P0_4-Pad10)
- U26 pad 11: unconnected-(U26-P0_5-Pad11) -> /USBSEL
- U26 pad 16: unconnected-(U26-P1_6-Pad16) -> /GPIO/TLS2
- U26 pad 17: unconnected-(U26-P1_7-Pad17) -> /GPIO/TLS1
- U3 pad 12: /USB/~{QON} -> /~{QON}
- U3 pad 15: /USB/VSYS -> /VSYS
- U3 pad 16: /USB/VSYS -> /VSYS
- U3 pad 23: unconnected-(U3-PMID-Pad23) -> /USB/PMID
- U3 pad 7: unconnected-(U3-INT-Pad7) -> /~{INT_SYS}
- U3 pad 8: unconnected-(U3-OTG-Pad8) -> /USB/PMIC_OTG
- U30 pad 4: /USB- -> /DEV_USB-
- U30 pad 5: /USB+ -> /DEV_USB+
- U30 pad 6: /USB+ -> /DEV_USB+
- U30 pad 7: /USB- -> /DEV_USB-
- U4 pad 1: unconnected-(U4-A0-Pad1) -> 3V3_SYS
- U4 pad 19: unconnected-(U4-SD7-Pad19) -> /SDA_SYS
- U4 pad 2: unconnected-(U4-A1-Pad2) -> 3V3_SYS
- U4 pad 20: unconnected-(U4-SC7-Pad20) -> /SCL_SYS
- U4 pad 21: unconnected-(U4-A2-Pad21) -> 3V3_SYS
- U4 pad 22: unconnected-(U4-SCL-Pad22) -> /SCL_HOST
- U4 pad 23: unconnected-(U4-SDA-Pad23) -> /SDA_HOST
- U4 pad 24: unconnected-(U4-VCC-Pad24) -> 3V3_SYS
- U4 pad 3: unconnected-(U4-~{RESET}-Pad3) -> /I2C_RESET
- U4 pad 4: /SDA_SYS -> /SDA_TOP
- U4 pad 5: /SCL_SYS -> /SCL_TOP
- U43 pad 1: /USB/VSYS -> /VSYS
- U43 pad 6: /USB/VSYS -> /VSYS
- U5 pad 1: unconnected-(U5-TXD-Pad1) -> Net-(J8-CC2)
- U5 pad 2: GND -> /USB/PMID
- U5 pad 3: Net-(U5-VDD) -> 3V3_SYS
- U5 pad 4: unconnected-(U5-RXD-Pad4) -> 3V3_SYS
- U5 pad 5: unconnected-(U5-SHDN-Pad5) -> /~{INT_SYS}
- U5 pad 6: unconnected-(U5-CANL-Pad6) -> /SDA_TOP
- U5 pad 7: Net-(U5-CANH) -> /SCL_TOP
- U5 pad 8: Net-(U5-RS) -> GND
- U7 pad 1: unconnected-(U7-SDO/ADDR-Pad1) -> GND
- U7 pad 11: unconnected-(U7-NC-Pad11) -> 3V3_SYS
- U7 pad 12: unconnected-(U7-SCLK/SCL-Pad12) -> /SCL_SYS
- U7 pad 2: unconnected-(U7-SDI/SDA-Pad2) -> /SDA_SYS
- U7 pad 3: unconnected-(U7-IO_VDD-Pad3) -> 3V3_SYS
- U7 pad 4: unconnected-(U7-TRIG-Pad4) -> GND
- U7 pad 7: unconnected-(U7-VDD-Pad7) -> 3V3_SYS
- U7 pad 9: unconnected-(U7-GND-Pad9) -> GND
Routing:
- net /~{INT_SYS}: track 104.1 -> 248.3 mm, vias 5 -> 14
- net /ESP_TXD: track 0.00 -> 117.6 mm, vias 0 -> 9
- net /~{BOOTLOADER}: track 0.00 -> 112.7 mm, vias 0 -> 5
- net /ESP_RXD: track 0.00 -> 112.2 mm, vias 0 -> 9
- net /~{ESPRESET}: track 0.00 -> 106.9 mm, vias 0 -> 6
- net 3V3_SYS: track 369.7 -> 473.3 mm, vias 25 -> 39
- net /USB/PMID: track 0.00 -> 97.4 mm, vias 0 -> 9
- net /SDA_TOP: track 0.00 -> 90.4 mm, vias 0 -> 2
- net /SCL_TOP: track 0.00 -> 89.6 mm, vias 0 -> 2
- net GND: track 218.6 -> 303.9 mm, vias 127 -> 200
- net /I2C_RESET: track 0.00 -> 81.1 mm, vias 0 -> 2
- net /USBSEL: track 0.00 -> 78.8 mm, vias 0 -> 4
- net /SCL_HOST: track 0.00 -> 75.7 mm, vias 0 -> 2
- net /SDA_HOST: track 0.00 -> 75.0 mm, vias 0 -> 2
- net unconnected-(U24-P0_1-Pad6): track 12.6 -> 72.2 mm, vias 1 -> 3
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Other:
- board text added: "+"
